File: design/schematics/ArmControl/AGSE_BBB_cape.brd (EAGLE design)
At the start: 71.8 x 54.6 mm, 53 parts, among them Q1 PFET-FQP27P06, Q2 PFET-FQP27P06, Q3 NFET-FQP30N06L, Q4 NFET-FQP30N06L, Q5 PFET-FQP27P06, Q6 PFET-FQP27P06, Q7 NFET-FQP30N06L, Q8 NFET-FQP30N06L, T1 2N3904, T2 2N3904, T3 2N3904, T4 2N3904, T5 2N3904, T6 2N3904, U1 V_REG_LD1085D2

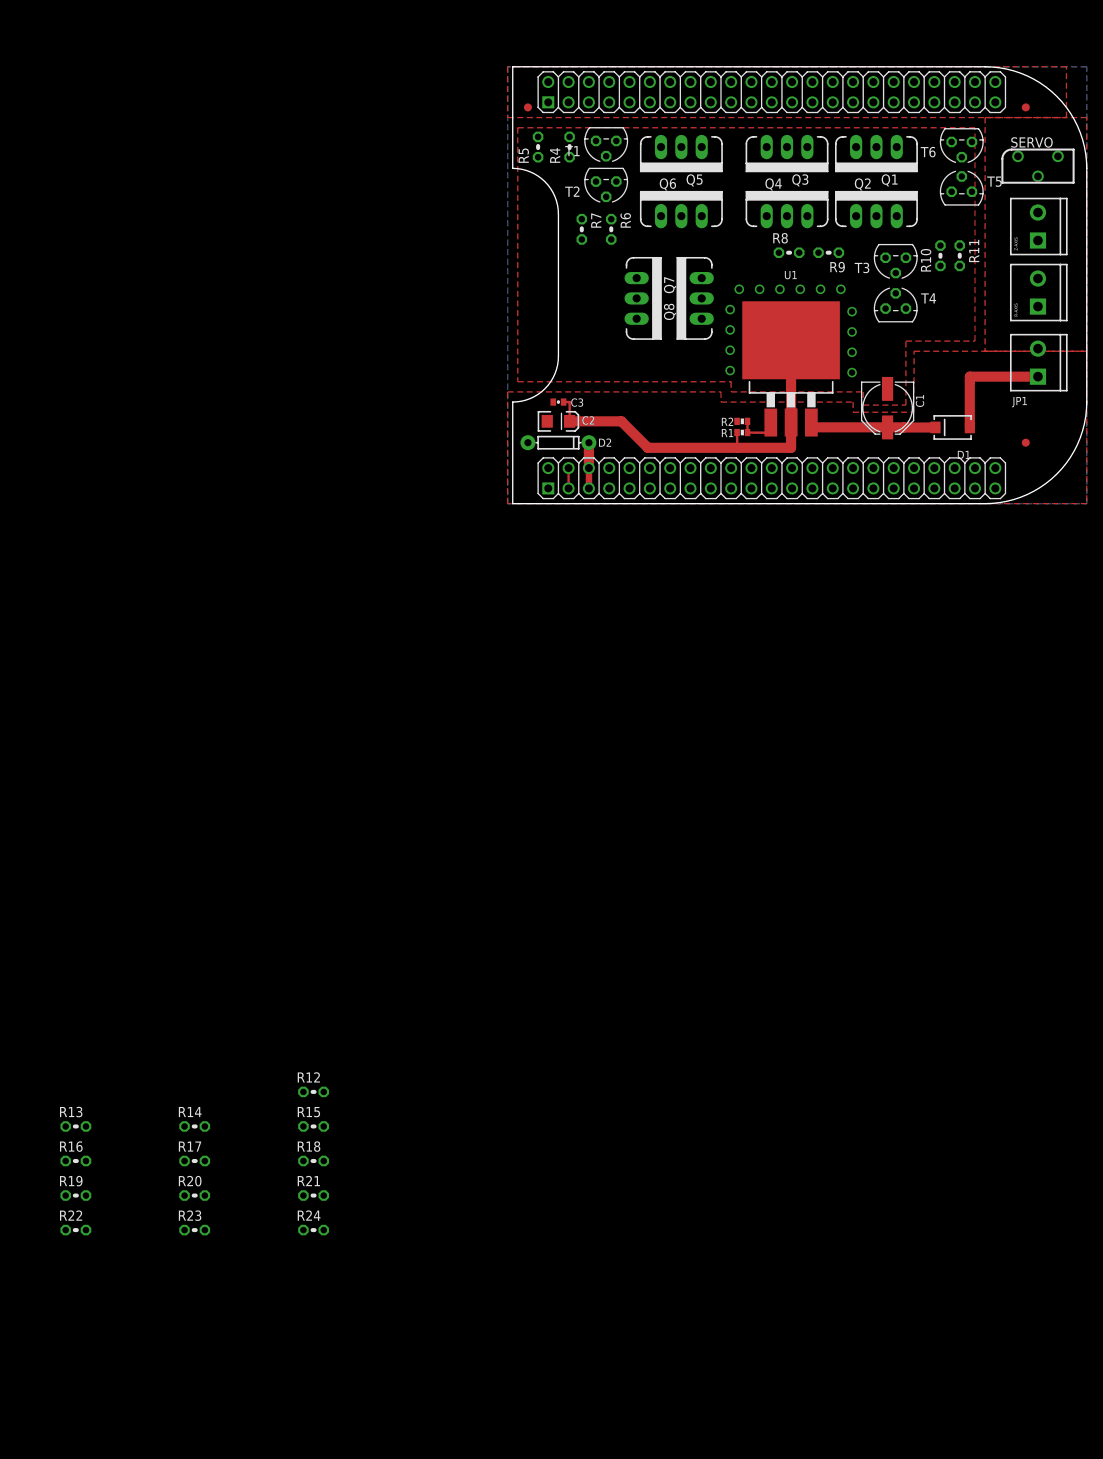
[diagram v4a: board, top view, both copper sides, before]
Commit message: changed to SMD.  working on placement & routing
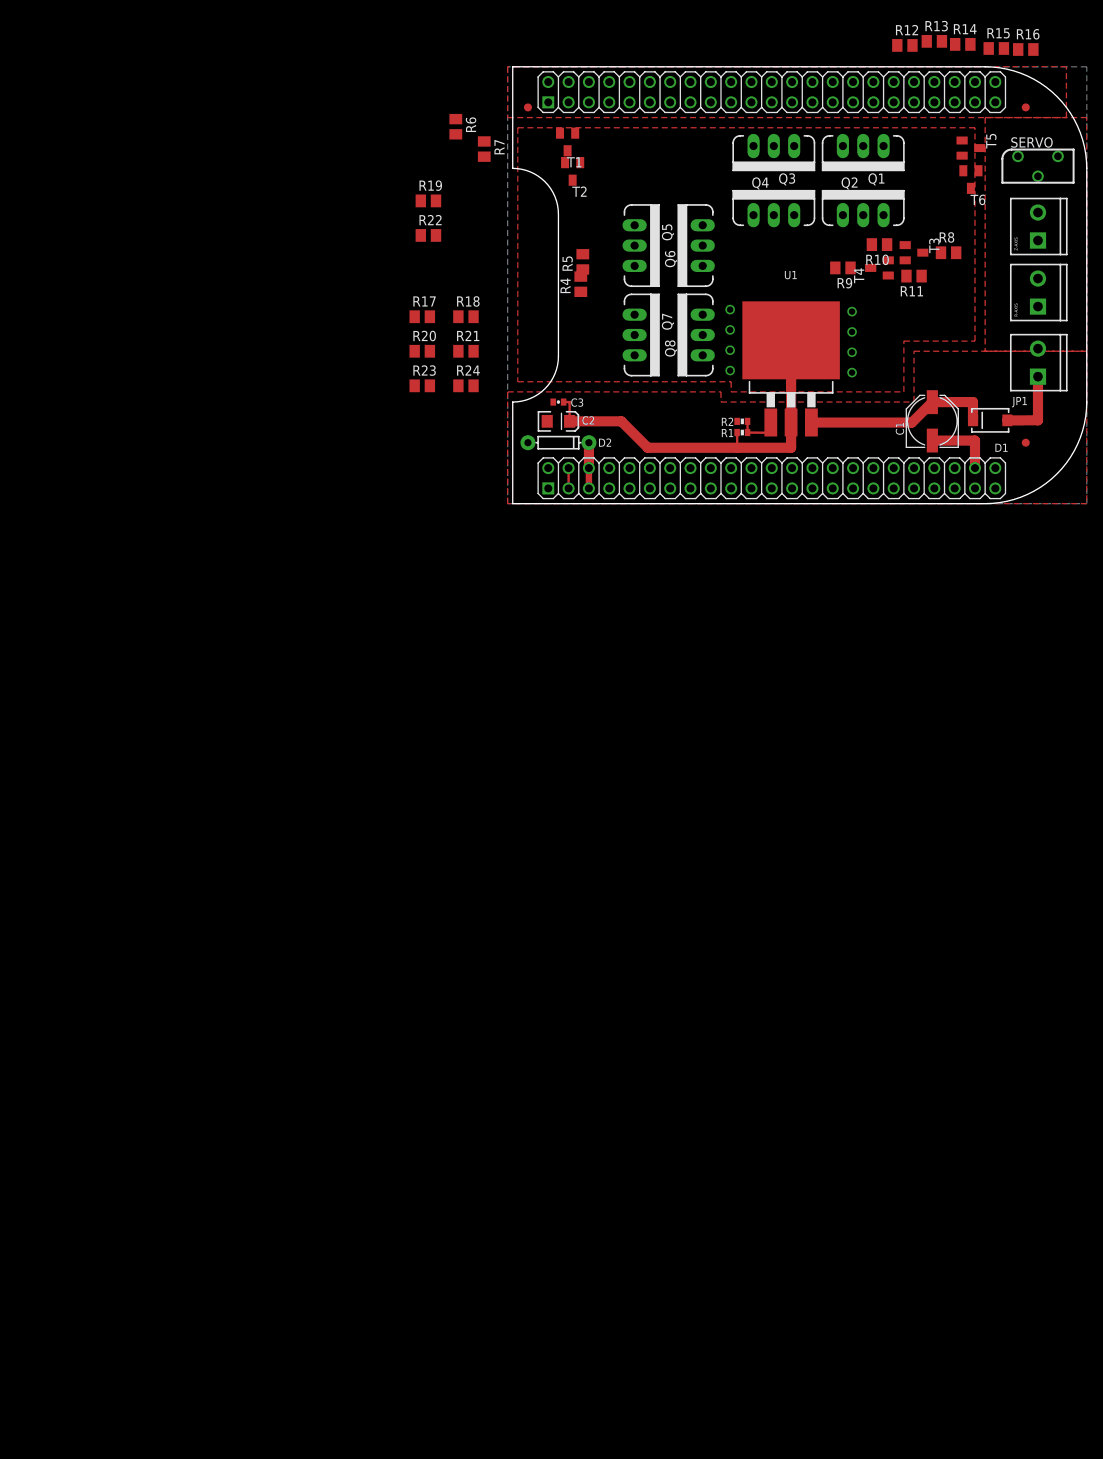
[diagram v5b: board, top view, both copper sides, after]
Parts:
- R10, R11, R12, R13, R14, R15, R16, R17, R18, R19, R20, R21, R22, R23, R24, R4, R5, R6, R7, R8, R9: device resistor:0204V -> resistor:M0805
- T1, T2, T3, T4, T5, T6: value 2N3904 -> (none); device transistor:TO92 -> transistor:SOT23-BEC
- moved R16 182.8 mm to (81.3, 59.3)
- moved R13 173.0 mm to (69.8, 60.3)
- moved R14 165.9 mm to (73.4, 59.9)
- moved R15 159.5 mm to (77.6, 59.4)
- moved R12 150.2 mm to (66.2, 59.8)
- moved R19 131.9 mm to (6.60, 40.4)
- moved R22 131.9 mm to (6.60, 36.1)
- moved R17 109.3 mm to (5.84, 25.9)
- moved R20 109.3 mm to (5.84, 21.6)
- moved R23 109.3 mm to (5.84, 17.3)
- moved R18 107.2 mm to (11.3, 25.9)
- moved R21 107.2 mm to (11.3, 21.6)
- moved R24 107.2 mm to (11.3, 17.3)
- moved R6 23.3 mm to (10.0, 49.7)
- moved R8 19.9 mm to (71.6, 33.9)
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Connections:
- net GND: now also T1.E, T2.E, T3.E, T4.E, T5.E, T6.E; no longer T1.3, T2.3, T3.3, T4.3, T5.3, T6.3
- net N$10: now also T2.B; no longer T2.2
- net N$13: now also T3.C; no longer T3.1
- net N$14: now also T4.C; no longer T4.1
- net N$15: now also T3.B; no longer T3.2
- net N$16: now also T4.B; no longer T4.2
- net N$17: now also T5.B; no longer T5.2
- net N$18: now also T5.C, T6.B; no longer T5.1, T6.2
- net N$7: now also T1.C; no longer T1.1
- net N$8: now also T2.C; no longer T2.1
- net N$9: now also T1.B; no longer T1.2
- net SERVO_TX/RX: now also T6.C; no longer T6.1
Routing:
- net GND: track 0.00 -> 8.78 mm
- net N$3: track 16.1 -> 23.5 mm
- net 12V: track 14.9 -> 9.29 mm
- net VOUT: vias 14 -> 8

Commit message: Working on board design, routing signals
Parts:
- moved R12 40.7 mm to (64.5, 19.2)
- moved R14 39.2 mm to (64.5, 21.7), turned to 180 degrees
- moved R13 34.6 mm to (68.5, 25.8), turned to 270 degrees
- moved R16 34.5 mm to (73.2, 25.8), turned to 270 degrees
- moved R15 34.3 mm to (70.9, 25.8), turned to 90 degrees
- moved T5 23.4 mm to (64.6, 25.8), turned to 90 degrees
- moved R5 16.5 mm to (39.2, 42.4)
- moved T6 16.0 mm to (65.0, 30.1), turned to 270 degrees
- moved R6 15.8 mm to (25.4, 46.1)
- moved R4 15.8 mm to (35.3, 42.4)
- moved R7 15.6 mm to (29.2, 46.4)
- moved T1 15.5 mm to (39.5, 47.0)
- moved R11 11.3 mm to (56.0, 30.0)
- moved R9 11.3 mm to (47.1, 31.0)
- moved T3 11.3 mm to (56.0, 32.9)
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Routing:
- net SERVO_TX/RX: track 0.00 -> 46.7 mm
- net BBB_RX: track 0.00 -> 36.0 mm, vias 0 -> 1
- net BBB_TX: track 0.00 -> 29.4 mm, vias 0 -> 1
- net 12V: track 9.29 -> 35.9 mm
- net GND: track 8.78 -> 22.8 mm, vias 0 -> 2
- net N$18: track 0.00 -> 13.8 mm
- net N$17: track 0.00 -> 3.23 mm
- net VOUT: track 47.5 -> 49.2 mm
- net N$3: track 23.5 -> 21.9 mm
- net N$4: track 5.57 -> 6.10 mm
- added copper zone on layer 16, net 12V

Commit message: working on routing
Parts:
- moved R6 16.3 mm to (41.7, 46.9), turned to 0 degrees
- moved R7 12.5 mm to (41.7, 44.8), turned to 180 degrees
- moved Z-AXIS 8.25 mm to (82.8, 27.2)
- moved R-AXIS 8.13 mm to (82.8, 35.3)
- moved R5 5.78 mm to (33.5, 41.5), turned to 0 degrees
- moved R4 2.45 mm to (37.6, 41.5), turned to 180 degrees
- moved T1 2.29 mm to (37.3, 46.2)
- moved T2 1.93 mm to (33.3, 46.2)
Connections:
- net N$1 renamed Z-
- net N$11 renamed R-
- net N$12 renamed R+
- net N$6 renamed Z+
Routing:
- net 12V: track 35.9 -> 136.4 mm, vias 0 -> 2
- net GND: track 22.8 -> 105.1 mm
- net Z+: track 0.00 -> 66.6 mm
- net Z-: track 0.00 -> 58.9 mm
- net N$13: track 0.00 -> 58.6 mm, vias 0 -> 2
- net R+: track 0.00 -> 52.3 mm
- net N$8: track 0.00 -> 41.8 mm, vias 0 -> 1
- net R-: track 0.00 -> 41.8 mm
- net N$7: track 0.00 -> 28.1 mm
- net N$14: track 0.00 -> 27.1 mm, vias 0 -> 1
- net +RADIUS: track 0.00 -> 23.6 mm, vias 0 -> 1
- net +HEIGHT: track 0.00 -> 22.6 mm, vias 0 -> 1
- net -RADIUS: track 0.00 -> 21.5 mm, vias 0 -> 1
- net -HEIGHT: track 0.00 -> 19.0 mm, vias 0 -> 1
- net N$10: track 0.00 -> 7.53 mm
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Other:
- board text added: "- 12V +"
- board text added: "R AXIS"
- board text added: "Z AXIS"
- board text removed: "+"
- board text removed: "-"
- board text removed: "12V"
- board text removed: "R-AXIS"
- board text removed: "Z-AXIS"

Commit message: working on routing the cape
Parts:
- moved R23 35.3 mm to (26.0, 46.2), turned to 90 degrees
- moved R24 31.7 mm to (24.1, 46.2), turned to 90 degrees
- moved R20 30.5 mm to (28.8, 41.7), turned to 90 degrees
- moved R21 27.0 mm to (22.2, 46.2), turned to 90 degrees
- moved R17 26.3 mm to (26.9, 41.7), turned to 90 degrees
- moved R19 21.8 mm to (30.7, 41.7), turned to 90 degrees
- moved R18 20.9 mm to (25.0, 41.7), turned to 90 degrees
- moved R22 20.5 mm to (20.3, 46.2), turned to 90 degrees
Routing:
- net GND: track 105.1 -> 325.6 mm, vias 2 -> 6
- net BBB_EQEP1B: track 0.00 -> 64.4 mm, vias 0 -> 1
- net BBB_EQEP1A: track 0.00 -> 58.0 mm
- net 12V: track 136.4 -> 161.2 mm
- net BBB_EQEP2A: track 0.00 -> 20.7 mm, vias 0 -> 1
- net BBB_EQEP2B: track 0.00 -> 14.0 mm, vias 0 -> 1
- net N$8: track 41.8 -> 35.9 mm
- net N$14: track 27.1 -> 29.7 mm
- net N$13: track 58.6 -> 59.4 mm
- net R-: track 41.8 -> 41.0 mm
